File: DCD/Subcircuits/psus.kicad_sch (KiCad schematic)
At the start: 0 parts

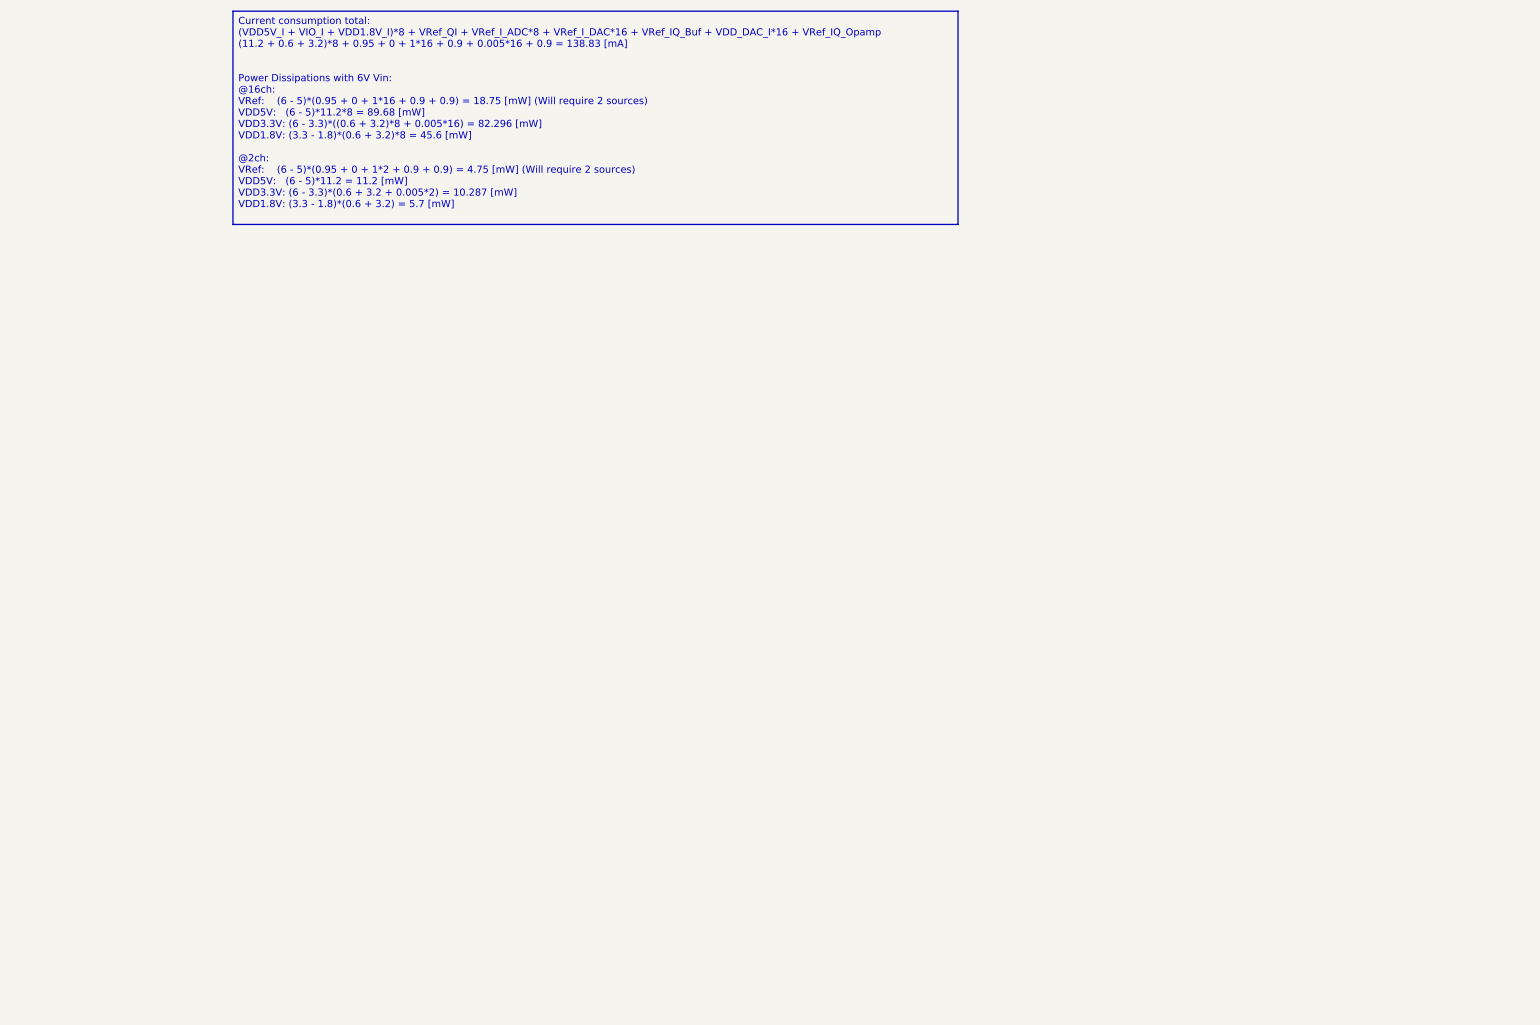
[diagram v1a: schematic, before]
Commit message: Added PSUS, progress on the PSU circuit design, slight tweaks to the rest
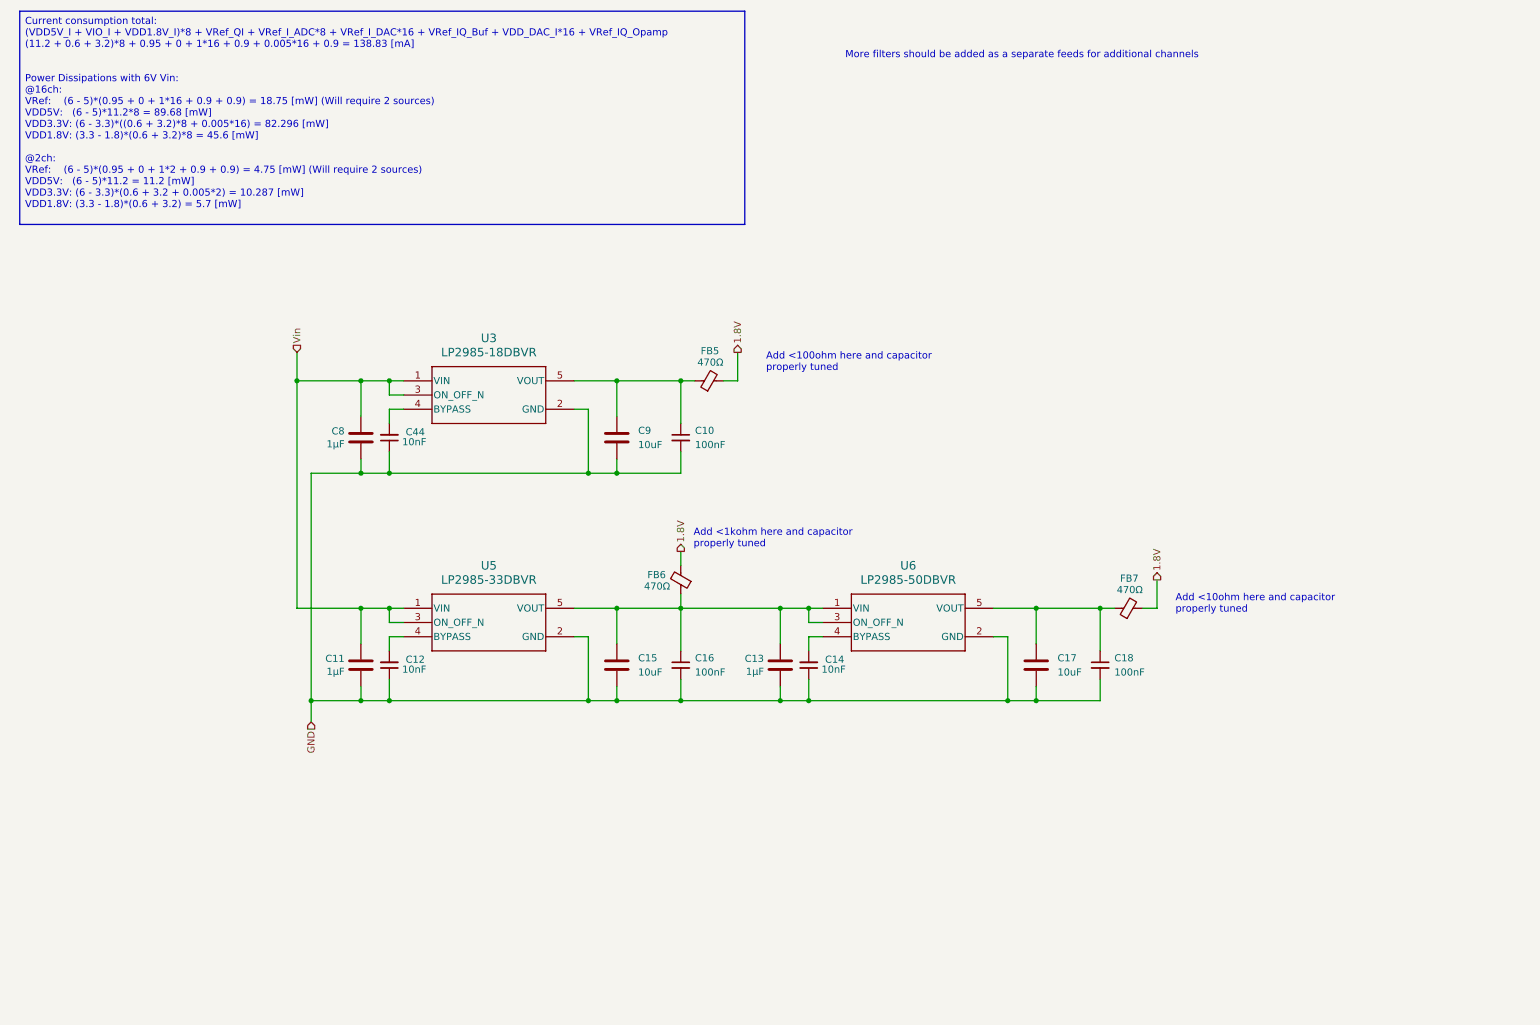
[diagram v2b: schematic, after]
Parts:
- added C10, C16, C18: 100nF, Capacitor_SMD:C_0603_1608Metric, symbol Device:C_Small
- added C11, C13, C8: 1µF, Capacitor_SMD:C_0603_1608Metric, symbol Device:C
- added C12, C14, C44: 10nF, Capacitor_SMD:C_0603_1608Metric, symbol Device:C_Small
- added C15, C17, C9: 10uF, Capacitor_SMD:C_1210_3225Metric, symbol Device:C
- added FB5, FB6, FB7: 470Ω, Inductor_SMD:L_0603_1608Metric, symbol Device:FerriteBead_Small
- added U3: LP2985-18DBVR, DBV0005A_N, symbol custom_components:LP2985-18DBVR
- added U5: LP2985-33DBVR, DBV0005A_N, symbol custom_components:LP2985-18DBVR
- added U6: LP2985-50DBVR, DBV0005A_N, symbol custom_components:LP2985-18DBVR
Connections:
- new net: C13.1, C15.1, C16.1, FB6.1, U5.5 (VOUT), U6.1 (VIN), U6.3 (ON_OFF_N)
- new net: C12.2, U5.4 (BYPASS)
- new net: C10.1, C9.1, FB5.1, U3.5 (VOUT)
- new net: C17.1, C18.1, FB7.1, U6.5 (VOUT)
- new net: C14.2, U6.4 (BYPASS)
- new net: C44.2, U3.4 (BYPASS)
- new net 1.8V: FB5.2, FB6.2, FB7.2
- new net GND: C10.2, C11.2, C12.1, C13.2, C14.1, C15.2, C16.2, C17.2, C18.2, C44.1, C8.2, C9.2, U3.2 (GND), U5.2 (GND), U6.2 (GND)
- new net Vin: C11.1, C8.1, U3.1 (VIN), U3.3 (ON_OFF_N), U5.1 (VIN), U5.3 (ON_OFF_N)
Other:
- note added: "Add <100ohm here and capacitor properly tuned"
- note added: "Add <10ohm here and capacitor properly tuned"
- note added: "Add <1kohm here and capacitor properly tuned"
- note added: "More filters should be added as a separate feeds for additional channels"

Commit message: Finished the schematics. Fixed the comments that we recieved
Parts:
- added FB1: 470Ω, Inductor_SMD:L_0603_1608Metric, symbol Device:FerriteBead_Small
- renumbered C8 to C1, C12 to C10, C15 to C11, C16 to C12, C13 to C2, C44 to C3, C14 to C4, C9 to C5, C17 to C6, C10 to C7, C18 to C8, C11 to C9, FB7 to FB2, FB5 to FB3, FB6 to FB4, U3 to U1, U6 to U2, U5 to U3
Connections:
- net 1.8V: no longer FB2.2, FB4.2
- net Vin: now also C2.1, U2.1 (VIN), U2.3 (ON_OFF_N); no longer C9.1, U3.1 (VIN), U3.3 (ON_OFF_N)
- net at C11.1, C12.1, FB4.1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: no longer C2.1, U2.1 (VIN), U2.3 (ON_OFF_N)
- net at C5.1, C7.1, FB3.1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: now also FB1.1
- net at C6.1, C8.1, FB2.1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: now also C9.1, U3.1 (VIN), U3.3 (ON_OFF_N)
- new net 3.3V: FB4.2
- new net 5V: FB2.2
- new net VIO: FB1.2
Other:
- note removed: "Add <100ohm here and capacitor properly tuned"
- note removed: "Add <10ohm here and capacitor properly tuned"
- note removed: "Add <1kohm here and capacitor properly tuned"
- moved on the sheet: C10, C11, C12, C2, C4, C6, C8, C9, FB2, FB4, U2, U3

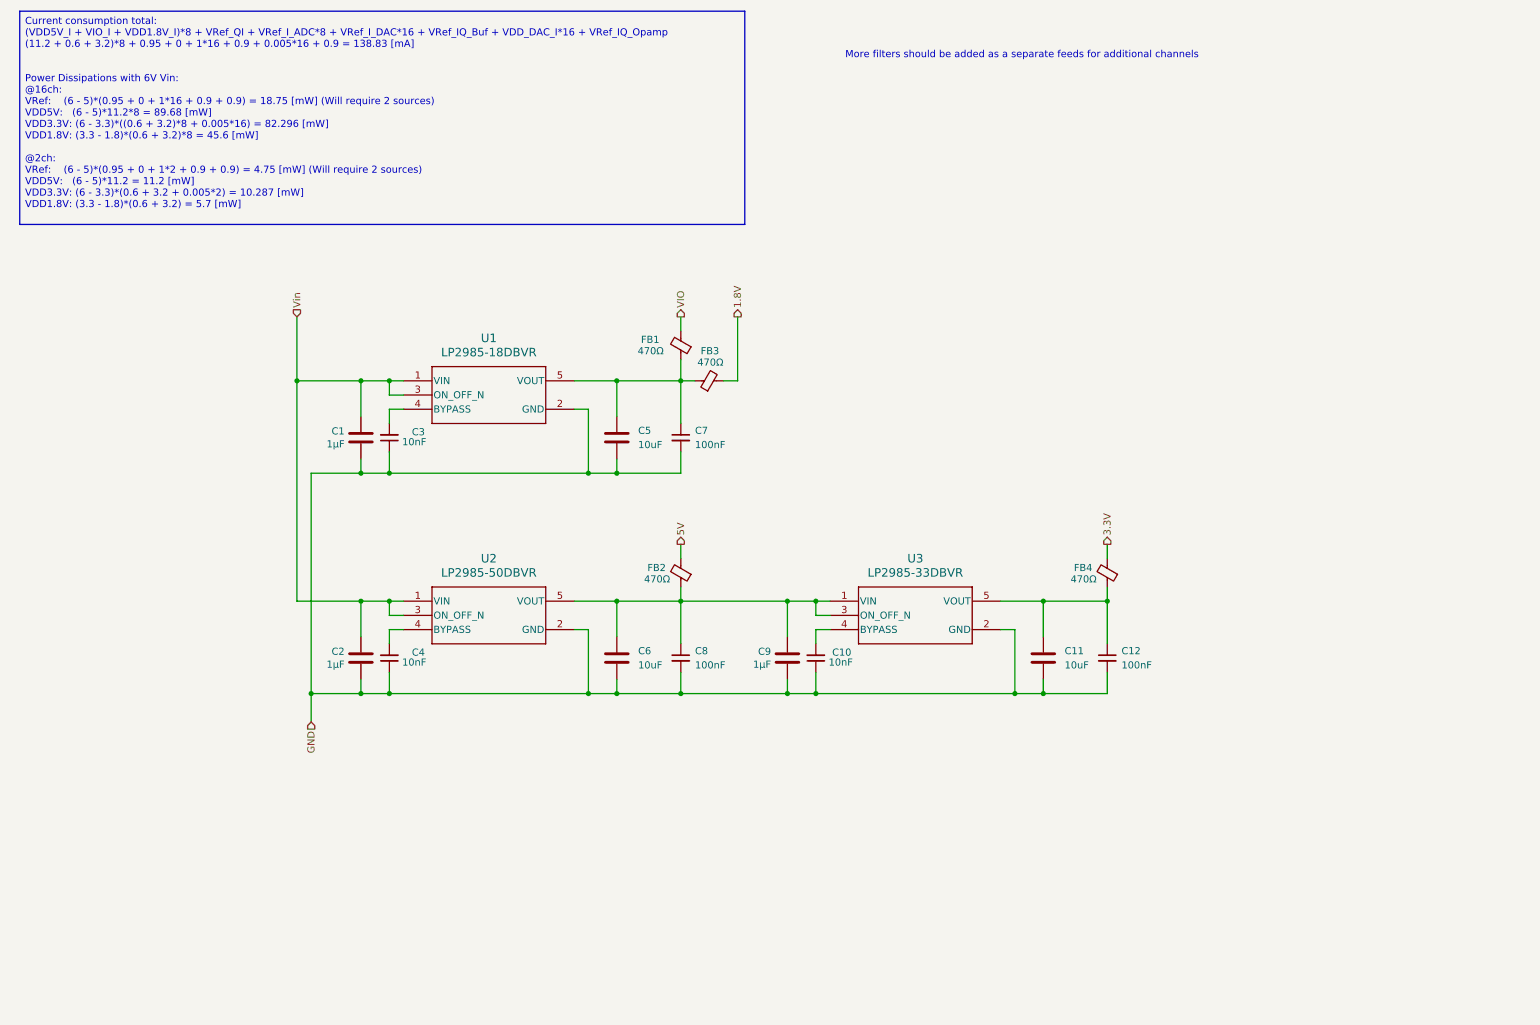
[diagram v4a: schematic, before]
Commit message: Finished
Final touches, PSUs filtering, external connections, psu connections for
the negative voltage, and the DAC higher voltage, and the negative
voltage. Added an external connection directely to the DAC.
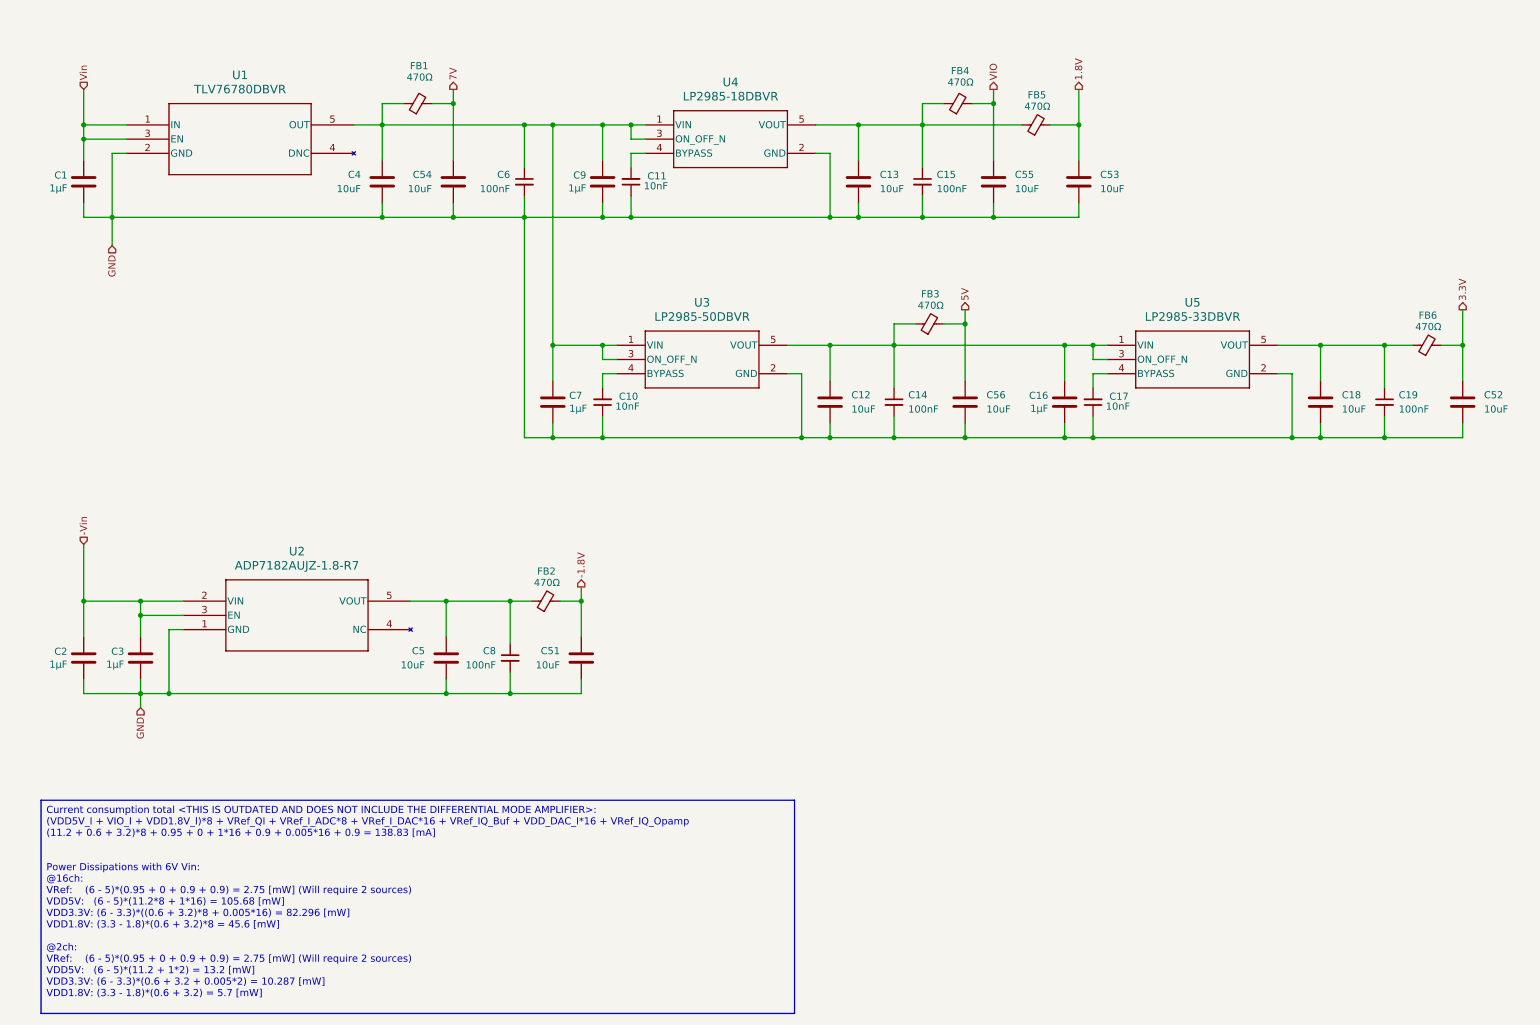
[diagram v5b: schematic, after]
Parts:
- added C1, C2, C3: 1µF, Capacitor_SMD:C_0603_1608Metric, symbol Device:C
- added C4, C5, C51, C52, C53, C54, C55, C56: 10uF, Capacitor_SMD:C_1210_3225Metric, symbol Device:C
- added C6, C8: 100nF, Capacitor_SMD:C_0603_1608Metric, symbol Device:C_Small
- added FB1, FB2: 470Ω, Inductor_SMD:L_0603_1608Metric, symbol Device:FerriteBead_Small
- added U1: TLV76780DBVR, SOT_80DBVR_TEX, symbol custom_components:TLV76780DBVR
- added U2: ADP7182AUJZ-1.8-R7, UJ-5_ADI, symbol custom_components:ADP7182AUJZ-1.8-R7
- renumbered C4 to C10, C3 to C11, C6 to C12, C5 to C13, C8 to C14, C7 to C15, C9 to C16, C10 to C17, C11 to C18, C12 to C19, C2 to C7, C1 to C9, FB2 to FB3, FB1 to FB4, FB3 to FB5, FB4 to FB6, U2 to U3, U1 to U4, U3 to U5
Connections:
- net 1.8V: now also C53.1
- net 3.3V: now also C52.1
- net 5V: now also C56.1
- net GND: now also C1.2, C2.2, C3.2, C4.2, C5.2, C51.2, C52.2, C53.2, C54.2, C55.2, C56.2, C6.2, C8.2, U1.2 (GND), U2.1 (GND)
- net VIO: now also C55.1
- net Vin: now also C1.1, U1.1 (IN), U1.3 (EN); no longer C7.1, C9.1, U3.1 (VIN), U3.3 (ON_OFF_N), U4.1 (VIN), U4.3 (ON_OFF_N)
- new net: C5.1, C8.1, FB2.1, U2.5 (VOUT)
- new net: C4.1, C6.1, C7.1, C9.1, FB1.1, U1.5 (OUT), U3.1 (VIN), U3.3 (ON_OFF_N), U4.1 (VIN), U4.3 (ON_OFF_N)
- new net -1.8V: C51.1, FB2.2
- new net -Vin: C2.1, C3.1, U2.2 (VIN), U2.3 (EN)
- new net 7V: C54.1, FB1.2
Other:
- note removed: "More filters should be added as a separate feeds for additional channels"
- moved on the sheet: C10, C11, C12, C13, C14, C15, C16, C17, C18, C19, C7, C9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
